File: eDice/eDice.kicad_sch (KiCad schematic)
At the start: 25 parts, among them Q1 PMOS, Q2 PN2222A, Q3 PN2222A, SW1 SW_Push, U1 NE555P, U10 4511, U11 SM420561N, U12 4029, U2 4029, U3 4511, U4 SM420561N

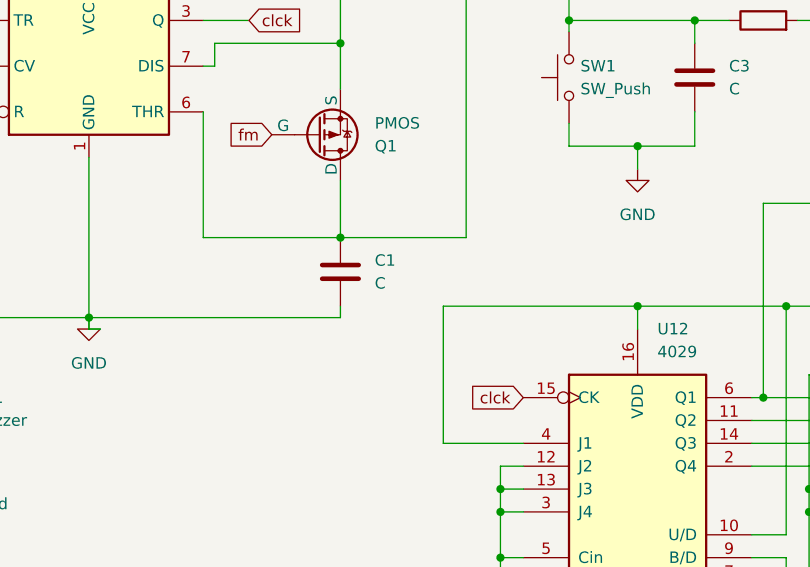
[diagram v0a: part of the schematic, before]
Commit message: rename nixie edice
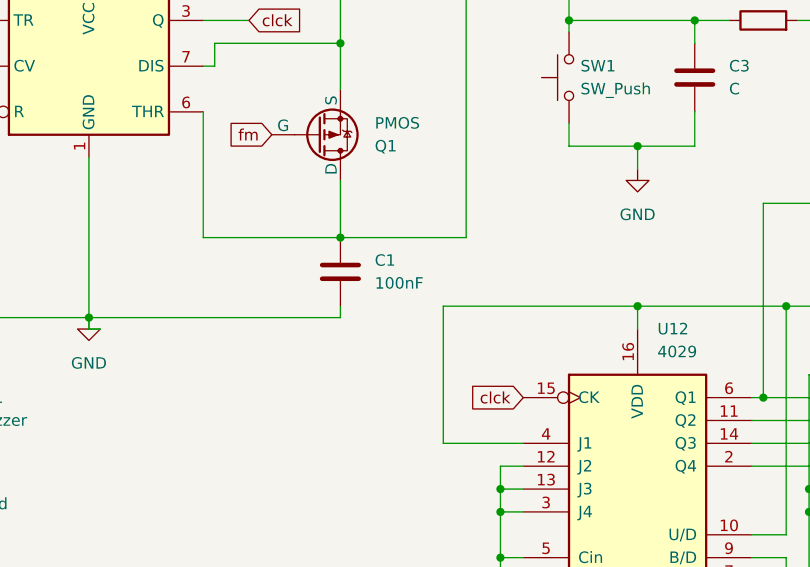
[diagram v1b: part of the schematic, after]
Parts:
- C1: value C -> 100nF; footprint (none) -> Capacitor_THT:C_Disc_D4.3mm_W1.9mm_P5.00mm
- C2: footprint (none) -> Capacitor_THT:C_Disc_D4.3mm_W1.9mm_P5.00mm
- C3, C4: footprint (none) -> Capacitor_THT:CP_Radial_D6.3mm_P2.50mm
- LS1: footprint (none) -> Buzzer_Beeper:Buzzer_D14mm_H7mm_P10mm
- Q1: footprint (none) -> Package_TO_SOT_THT:TO-92L_Inline
- R1, R10, R2, R3, R4, R5, R6: footprint (none) -> Resistor_THT:R_Axial_DIN0204_L3.6mm_D1.6mm_P5.08mm_Horizontal
- R8: footprint (none) -> Potentiometer_THT:Potentiometer_Runtron_RM-063_Horizontal
- SW1: footprint (none) -> Connector_PinSocket_2.54mm:PinSocket_1x02_P2.54mm_Vertical
- U10: footprint (none) -> Package_DIP:DIP-16_W7.62mm
- U12, U2, U3: footprint (none) -> Package_DIP:DIP-16_W7.62mm_Socket

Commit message: update: d6/20
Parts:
- removed Q2: PN2222A, Package_TO_SOT_THT:TO-92_Inline, symbol Transistor_BJT:PN2222A
- added D2: 1N4148, Diode_THT:D_DO-35_SOD27_P7.62mm_Horizontal, symbol Diode:1N4148
- added Q4, Q5, Q6: PN2222A, Package_TO_SOT_THT:TO-92_Inline, symbol Transistor_BJT:PN2222A
- added R12, R7: 10k, Resistor_THT:R_Axial_DIN0204_L3.6mm_D1.6mm_P5.08mm_Horizontal, symbol Device:R
- added SW2: SW_SPDT_321, symbol Switch:SW_SPDT_321
- R6: footprint Resistor_THT:R_Axial_DIN0204_L3.6mm_D1.6mm_P5.08mm_Horizontal -> (none)
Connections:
- net GND: now also R6.1; no longer R6.2
- net PE: now also R6.2, Q5.1 (E); no longer R6.1
- net vcc: now also D2.1 (K), SW2.3 (A)
- net at U10.7 (DA), U12.6 (Q1): now also Q3.3 (C), R4.2; no longer R4.1
- net at U10.1 (DB), U12.11 (Q2): now also R12.2
- net at U10.6 (DD), U12.2 (Q4): now also Q6.3 (C)
- new net: D2.2 (A), R7.1, SW2.1 (C)
- new net: Q5.2 (B), R7.2
- new net: Q4.1 (E), Q5.3 (C)
- new net: Q6.2 (B), R12.1
- new net: Q4.2 (B), R4.1
- new net: Q4.3 (C), Q6.1 (E)
- new net +5V: SW2.2 (B)
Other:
- moved on the sheet: Q3, R1, R10, R5, U10, U11, U12, U2, U3, U4

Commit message: edice
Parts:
- added D3: 1N4148, Diode_THT:D_DO-35_SOD27_P7.62mm_Horizontal, symbol Diode:1N4148
- added J1: power_sply, symbol Connector:Conn_01x02_Socket
- added Q2: PN2222A, Package_TO_SOT_THT:TO-92_Inline, symbol Transistor_BJT:PN2222A
- added R9: 10k, Resistor_THT:R_Axial_DIN0204_L3.6mm_D1.6mm_P5.08mm_Horizontal, symbol Device:R
- added U5: 3-5V boost, symbol eDiceLib:3-5v_boost
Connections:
- net GND: now also J1.1 (Pin_1), Q2.1 (E), U5.12 (out-); no longer R1.2
- net vcc: now also U5.12 (out-); no longer D2.1 (K), SW2.3 (A)
- net +5V: no longer names the net of SW2.2 (B)
- net +5V: now also J1.2 (Pin_2)
- new net: D3.2 (A), R9.1, SW2.3 (A)
- new net: Q2.2 (B), R9.2
- new net: Q2.3 (C), R1.2
- new net: D2.1 (K), D3.1 (K), U5.12 (out-)
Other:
- moved on the sheet: D2, R1, R6

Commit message: updates
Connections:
- net GND: no longer U10.3 (~{LT}), U10.4 (~{BI}), U3.3 (~{LT}), U3.4 (~{BI})
- net vcc: now also U10.3 (~{LT}), U10.4 (~{BI}), U2.10 (U/D), U2.16 (VDD), U3.16 (Vdd), U3.3 (~{LT}), U3.4 (~{BI})
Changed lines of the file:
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@@
   (junction (at 92.71 191.77) (diameter 0) (color 0 0 0 0)
   )
-  (junction (at 227.33 184.15) (diameter 0) (color 0 0 0 0)
-  )
   (junction (at 180.34 140.97) (diameter 0) (color 0 0 0 0)
   )
@@
   (junction (at 107.95 214.63) (diameter 0) (color 0 0 0 0)
   )
-  (junction (at 227.33 186.69) (diameter 0) (color 0 0 0 0)
-  )
   (junction (at 78.74 67.31) (diameter 0) (color 0 0 0 0)
   )
@@
   (junction (at 92.71 184.15) (diameter 0) (color 0 0 0 0)
   )
-  (junction (at 127 186.69) (diameter 0) (color 0 0 0 0)
-  )
   (junction (at 193.04 181.61) (diameter 0) (color 0 0 0 0)
   )
@@
   (junction (at 191.77 74.93) (diameter 0) (color 0 0 0 0)
   )
-  (junction (at 127 184.15) (diameter 0) (color 0 0 0 0)
-  )
   (junction (at 208.28 74.93) (diameter 0) (color 0 0 0 0)
   )
@@
   )
   (junction (at 224.79 163.83) (diameter 0) (color 0 0 0 0)
+  )
+  (junction (at 128.27 186.69) (diameter 0) (color 0 0 0 0)
+  )
+  (junction (at 228.6 186.69) (diameter 0) (color 0 0 0 0)
   )
   (no_connect (at 220.98 194.31))
@@
     (stroke (width 0) (type default))
   )
-  (wire (pts (xy 127 184.15) (xy 127 186.69))
-    (stroke (width 0) (type default))
-  )
   (wire (pts (xy 220.98 181.61) (xy 228.6 181.61))
     (stroke (width 0) (type default))
@@
     (stroke (width 0) (type default))
   )
+  (wire (pts (xy 128.27 184.15) (xy 128.27 186.69))
+    (stroke (width 0) (type default))
+  )
   (wire (pts (xy 208.28 209.55) (xy 208.28 214.63))
     (stroke (width 0) (type default))
@@
     (stroke (width 0) (type default))
   )
+  (wire (pts (xy 228.6 184.15) (xy 228.6 186.69))
+    (stroke (width 0) (type default))
+  )
   (wire (pts (xy 154.94 214.63) (xy 138.43 214.63))
     (stroke (width 0) (type default))
@@
     (stroke (width 0) (type default))
   )
-  (wire (pts (xy 227.33 171.45) (xy 227.33 184.15))
-    (stroke (width 0) (type default))
-  )
   (wire (pts (xy 50.8 77.47) (xy 50.8 76.2))
     (stroke (width 0) (type default))
   )
-  (wire (pts (xy 127 186.69) (xy 128.27 186.69))
-    (stroke (width 0) (type default))
-  )
   (wire (pts (xy 64.77 45.72) (xy 78.74 45.72))
     (stroke (width 0) (type default))
   )
-  (wire (pts (xy 127 171.45) (xy 127 184.15))
-    (stroke (width 0) (type default))
-  )
   (wire (pts (xy 95.25 181.61) (xy 92.71 181.61))
     (stroke (width 0) (type default))
@@
     (stroke (width 0) (type default))
   )
-  (wire (pts (xy 127 186.69) (xy 127 193.04))
+  (wire (pts (xy 127 171.45) (xy 127 193.04))
     (stroke (width 0) (type default))
   )
@@
     (stroke (width 0) (type default))
   )
+  (wire (pts (xy 228.6 186.69) (xy 228.6 190.5))
+    (stroke (width 0) (type default))
+  )
   (wire (pts (xy 123.19 130.81) (xy 170.18 130.81))
     (stroke (width 0) (type default))
@@
     (stroke (width 0) (type default))
   )
+  (wire (pts (xy 228.6 190.5) (xy 229.87 190.5))
+    (stroke (width 0) (type default))
+  )
   (wire (pts (xy 213.36 86.36) (xy 222.25 86.36))
     (stroke (width 0) (type default))
@@
     (stroke (width 0) (type default))
   )
-  (wire (pts (xy 227.33 184.15) (xy 228.6 184.15))
-    (stroke (width 0) (type default))
-  )
   (wire (pts (xy 92.71 19.05) (xy 92.71 67.31))
     (stroke (width 0) (type default))
@@
     (stroke (width 0) (type default))
   )
-  (wire (pts (xy 127 184.15) (xy 128.27 184.15))
-    (stroke (width 0) (type default))
-  )
   (wire (pts (xy 222.25 176.53) (xy 228.6 176.53))
     (stroke (width 0) (type default))
@@
     (stroke (width 0) (type default))
   )
+  (wire (pts (xy 128.27 186.69) (xy 128.27 190.5))
+    (stroke (width 0) (type default))
+  )
   (wire (pts (xy 170.18 186.69) (xy 170.18 189.23))
     (stroke (width 0) (type default))
@@
     (stroke (width 0) (type default))
   )
+  (wire (pts (xy 128.27 190.5) (xy 129.54 190.5))
+    (stroke (width 0) (type default))
+  )
   (wire (pts (xy 148.59 179.07) (xy 154.94 179.07))
     (stroke (width 0) (type default))
@@
     (stroke (width 0) (type default))
   )
-  (wire (pts (xy 227.33 186.69) (xy 228.6 186.69))
-    (stroke (width 0) (type default))
-  )
-  (wire (pts (xy 227.33 186.69) (xy 227.33 193.04))
+  (wire (pts (xy 227.33 171.45) (xy 227.33 193.04))
     (stroke (width 0) (type default))
   )
@@
   )
   (wire (pts (xy 248.92 184.15) (xy 255.27 184.15))
-    (stroke (width 0) (type default))
-  )
-  (wire (pts (xy 227.33 184.15) (xy 227.33 186.69))
     (stroke (width 0) (type default))
   )
@@
     )
   )
+  (global_label "vcc" (shape input) (at 129.54 190.5 0) (fields_autoplaced)
+    (effects (font (size 1.27 1.27)) (justify left))
+    (property "Intersheetrefs" "${INTERSHEET_REFS}" (at 135.67 190.5 0)
+      (effects (font (size 1.27 1.27)) (justify left) hide)
+    )
+  )
   (global_label "fm" (shape input) (at 133.35 43.18 0) (fields_autoplaced)
     (effects (font (size 1.27 1.27)) (justify left))
@@
     )
   )
+  (global_label "vcc" (shape input) (at 238.76 163.83 90) (fields_autoplaced)
+    (effects (font (size 1.27 1.27)) (justify left))
+    (property "Intersheetrefs" "${INTERSHEET_REFS}" (at 238.76 157.7 90)
+      (effects (font (size 1.27 1.27)) (justify left) hide)
+    )
+  )
   (global_label "clck" (shape input) (at 104.14 21.59 180) (fields_autoplaced)
     (effects (font (size 1.27 1.27)) (justify right))
@@
     )
   )
+  (global_label "vcc" (shape input) (at 229.87 190.5 0) (fields_autoplaced)
+    (effects (font (size 1.27 1.27)) (justify left))
+    (property "Intersheetrefs" "${INTERSHEET_REFS}" (at 236 190.5 0)
+      (effects (font (size 1.27 1.27)) (justify left) hide)
+    )
+  )

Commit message: ok
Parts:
- removed Q6: PN2222A, Package_TO_SOT_THT:TO-92_Inline, symbol Transistor_BJT:PN2222A
- removed R12: 10k, Resistor_THT:R_Axial_DIN0204_L3.6mm_D1.6mm_P5.08mm_Horizontal, symbol Device:R
- added D4: 1N4148, Diode_THT:D_DO-35_SOD27_P7.62mm_Horizontal, symbol Diode:1N4148
- added R11: 4.7k, symbol Device:R
- R1, R10: value R -> 1k
- R2: value R -> 47k; footprint Resistor_THT:R_Axial_DIN0204_L3.6mm_D1.6mm_P5.08mm_Horizontal -> (none)
- R4, R5, R7: value 10k -> 22k; footprint Resistor_THT:R_Axial_DIN0204_L3.6mm_D1.6mm_P5.08mm_Horizontal -> (none)
- R6: value 100k -> 22k
- R8: value R_Variable -> 100k
- R9: value 10k -> 4.7k; footprint Resistor_THT:R_Axial_DIN0204_L3.6mm_D1.6mm_P5.08mm_Horizontal -> (none)
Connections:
- net GND: now also R1.2, R9.2; no longer Q2.1 (E), R6.1
- net PE: now also D3.1 (K), R9.1, D4.1 (K); no longer Q3.1 (E), Q5.1 (E), R6.2
- net clck: now also R2.1; no longer D1.2 (A)
- net at C3.1, R3.1, SW1.2: now also D1.1 (K); no longer R2.2
- net at D2.2 (A), SW2.1 (C): now also Q4.3 (C); no longer R7.1
- net at R7.2: now also U2.11 (Q2), U3.1 (DB); no longer Q5.2 (B)
- net at Q3.2 (B): now also R5.1; no longer R5.2
- net at R4.2, U10.7 (DA), U12.6 (Q1): now also Q5.3 (C); no longer Q3.3 (C)
- net at Q4.1 (E): now also Q3.3 (C); no longer Q5.3 (C)
- net at U10.1 (DB), U12.11 (Q2): now also R5.2
- net at U10.2 (DC), U12.14 (Q3): now also R6.2
- net at Q2.2 (B): now also R6.1; no longer R9.2
- net at Q2.3 (C): now also Q3.1 (E); no longer R1.2
- net at C1.1, U1.2 (TR), U1.6 (THR): now also R11.2; no longer Q1.1 (D)
- new net: D3.2 (A), Q5.1 (E)
- new net: D1.2 (A), R2.2
- new net: D2.1 (K), SW2.3 (A), U5.12 (out-)
- new net: Q1.1 (D), R11.1
- new net: D4.2 (A), Q2.1 (E)
- new net: Q5.2 (B), R7.1
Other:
- moved on the sheet: D2, J1, LS1, Q1, R1, R10, SW2, U10, U11, U12, U2, U3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
